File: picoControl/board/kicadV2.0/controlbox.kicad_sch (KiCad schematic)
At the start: 85 parts, among them J1 lineOut1, J10 OLED, J11 CSRF, J12 MotorL, J13 MotorR, J14 lineOut1, J15 grove I2C, J16 R1, J17 L1, J18 JST-2-switch, J19 JST-2-switch, J2 Audio1, J20 DMX, J21 RJ45_LED_Shielded, J22 JST-2-switch, J23 PowerIn, J24 grove GPIO, J25 PowerIn, J3 R1, J4 L1, J5 APC220, J6 NRF24L01, J7 relay1, J8 relay2, J9 general, M1 Pico, SW1 RotaryEncoder_Switch, SW2 RF on-off, U1 PCA9685PW, U2 MAX485E, U3 LM7805_TO220, U4 fermion-mp3, U5 fermion-mp3

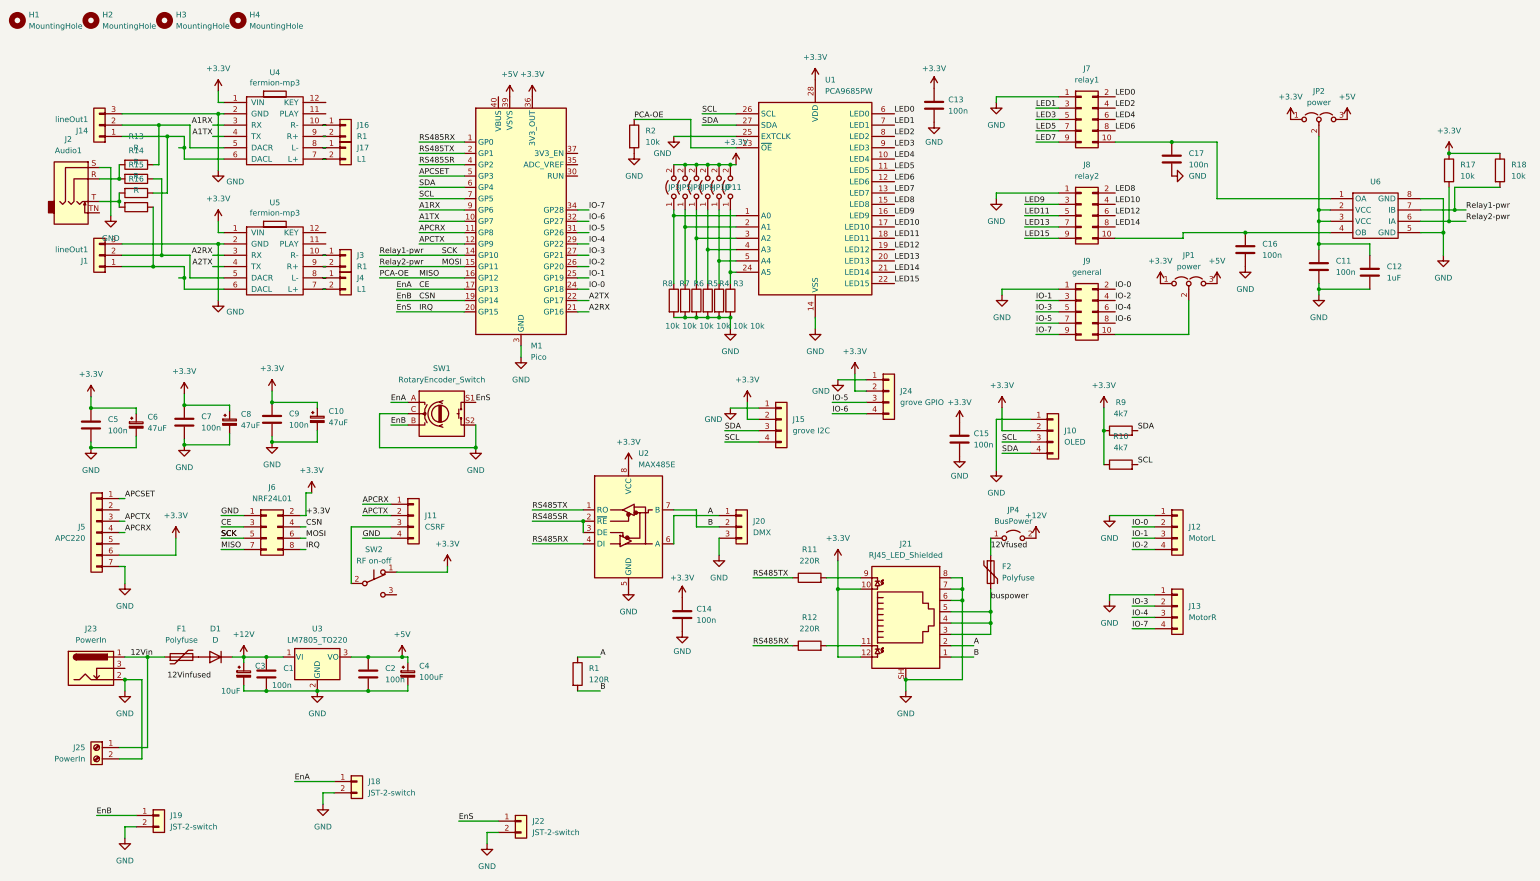
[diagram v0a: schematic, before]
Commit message: V2 board of picoCOntrol added
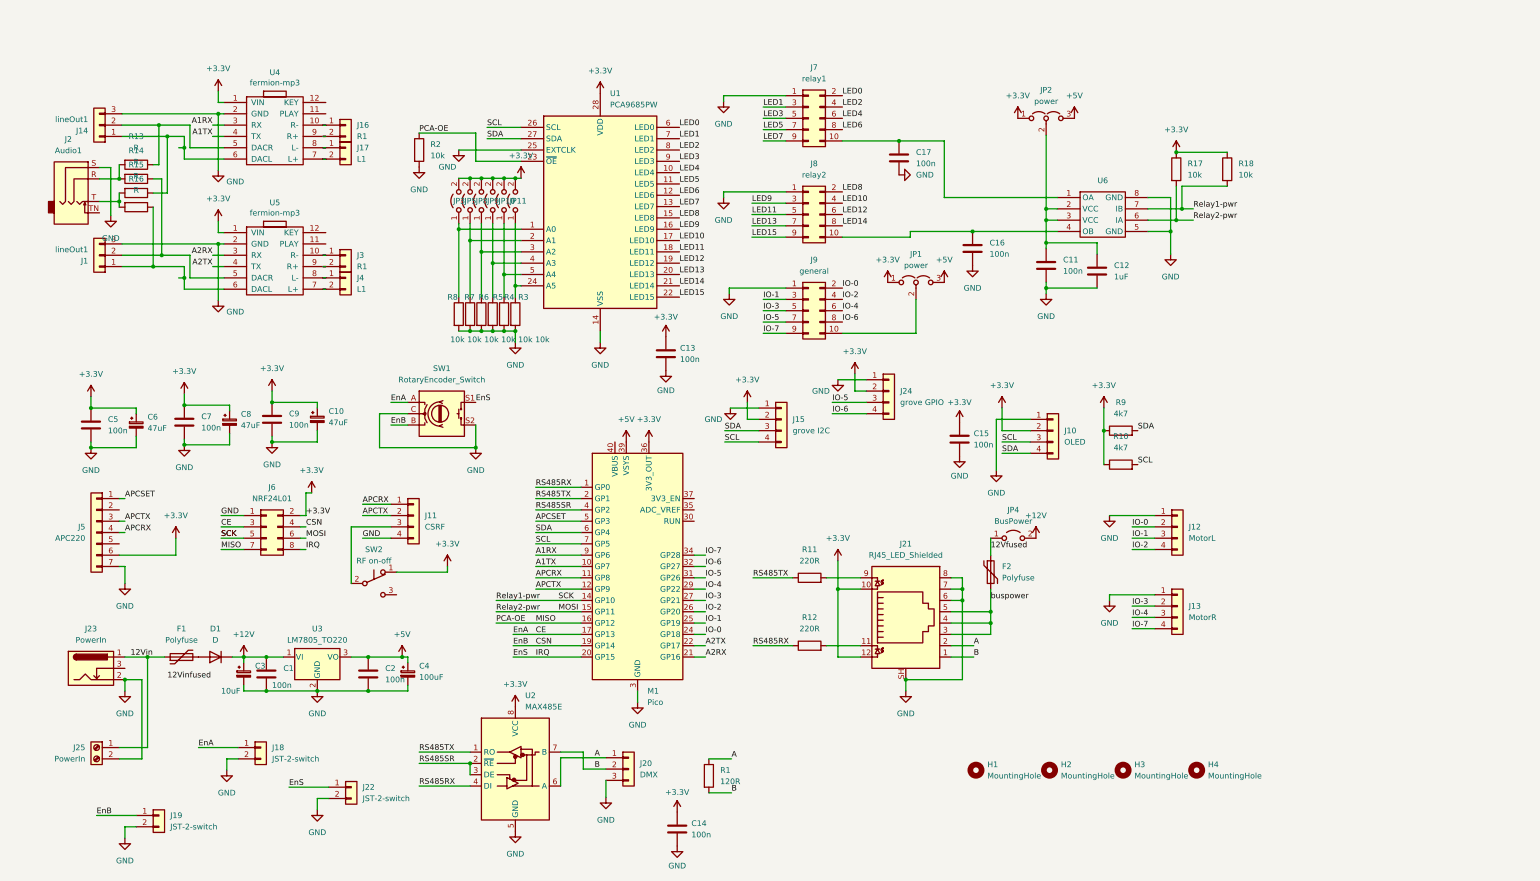
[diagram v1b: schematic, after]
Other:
- moved on the sheet: C11, C12, C13, C14, C16, C17, H1, H2, H3, H4, J18, J20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
